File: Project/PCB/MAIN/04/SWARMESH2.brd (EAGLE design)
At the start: 75 x 75 mm, 47 parts, among them Q1 TIP122, U1 ESP32DEVKITC, U2 CD4051BEE4, U3 L293D, U4 L7805CV-DG, U5 TCRT5000L, U6 TCRT5000L

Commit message: update pcb 20:33
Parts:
- moved C5 16.9 mm to (21.9, 46.1)
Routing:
- net GND: track 481.8 -> 491.5 mm
- net ADCMX: track 49.3 -> 50.7 mm
- added copper zone on layer 16, net GND
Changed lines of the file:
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@@
 <attribute name="VALUE" x="53.972809375" y="12.749940625" size="2.08328125" layer="27" ratio="10" rot="SR0" display="off"/>
 </element>
-<element name="C5" library="adafruit" library_urn="urn:adsk.eagle:library:420" package="C025-030X050" package3d_urn="urn:adsk.eagle:package:6240322/1" value="" x="38.3667" y="42.4053" smashed="yes" rot="R90">
-<attribute name="NAME" x="36.4617" y="40.1193" size="1.27" layer="25" font="vector" ratio="15" rot="R90"/>
-<attribute name="VALUE" x="41.4147" y="40.1193" size="1.27" layer="27" ratio="10" rot="R90"/>
+<element name="C5" library="adafruit" library_urn="urn:adsk.eagle:library:420" package="C025-030X050" package3d_urn="urn:adsk.eagle:package:6240322/1" value="" x="21.9075" y="46.0629" smashed="yes" rot="R90">
+<attribute name="NAME" x="20.0025" y="43.7769" size="1.27" layer="25" font="vector" ratio="15" rot="R90"/>
+<attribute name="VALUE" x="24.9555" y="43.7769" size="1.27" layer="27" ratio="10" rot="R90"/>
 </element>
 <element name="C3" library="adafruit" library_urn="urn:adsk.eagle:library:420" package="C025-025X050" package3d_urn="urn:adsk.eagle:package:6240323/1" value="" x="58.42" y="70.8025" smashed="yes">
@@
 <wire x1="12.6746" y1="34.8742" x2="13.87145" y2="34.8742" width="0.635" layer="16"/>
 <wire x1="13.87145" y1="34.8742" x2="13.895325" y2="34.898075" width="0.635" layer="16"/>
-<wire x1="13.208" y1="41.4975" x2="21.415" y2="49.7045" width="0.635" layer="16"/>
-<wire x1="21.2725" y1="53.0225" x2="21.415" y2="52.88" width="0.635" layer="16"/>
-<wire x1="21.415" y1="52.88" x2="21.415" y2="49.7045" width="0.635" layer="16"/>
+<wire x1="13.208" y1="41.4975" x2="13.208" y2="45.1551" width="0.635" layer="16"/>
+<wire x1="21.2725" y1="53.0225" x2="21.0754" y2="53.0225" width="0.635" layer="16"/>
+<wire x1="21.0754" y1="53.0225" x2="13.208" y2="45.1551" width="0.635" layer="16"/>
 <wire x1="52.695" y1="33.9825" x2="52.705" y2="33.9725" width="0.635" layer="16"/>
 <wire x1="52.695" y1="33.9825" x2="51.235" y2="33.9825" width="0.635" layer="16"/>
@@
 <wire x1="58.7375" y1="44.1325" x2="59.055" y2="44.45" width="0.635" layer="16"/>
 <wire x1="59.055" y1="44.45" x2="62.23" y2="44.45" width="0.635" layer="16"/>
-<wire x1="38.3667" y1="43.6753" x2="44.4627" y2="43.6753" width="0.635" layer="16"/>
-<wire x1="50.0099" y1="49.2225" x2="44.4627" y2="43.6753" width="0.635" layer="16"/>
-<wire x1="50.0099" y1="49.2225" x2="51.235" y2="49.2225" width="0.635" layer="16"/>
+<wire x1="24.4067" y1="51.0513" x2="21.9075" y2="48.5521" width="0.635" layer="16"/>
+<wire x1="21.9075" y1="48.5521" x2="21.9075" y2="47.3329" width="0.635" layer="16"/>
+<wire x1="24.4067" y1="51.0513" x2="27.432" y2="51.0513" width="0.635" layer="16"/>
 <wire x1="41.1675" y1="36.83" x2="42.8625" y2="36.83" width="0.3048" layer="16"/>
 <wire x1="42.8625" y1="36.83" x2="43.5423" y2="36.1502" width="0.3048" layer="16"/>
@@
 <wire x1="41.1675" y1="8.255" x2="41.1675" y2="9.5551375" width="0.3048" layer="16"/>
 <wire x1="41.1675" y1="9.5551375" x2="39.4192375" y2="11.3034" width="0.3048" layer="16"/>
-<wire x1="21.2725" y1="53.0225" x2="23.0886" y2="51.2064" width="0.6096" layer="16"/>
-<wire x1="34.7091" y1="43.6753" x2="38.3667" y2="43.6753" width="0.6096" layer="16"/>
-<wire x1="34.7091" y1="43.6753" x2="27.178" y2="51.2064" width="0.6096" layer="16"/>
-<wire x1="23.0886" y1="51.2064" x2="27.178" y2="51.2064" width="0.6096" layer="16"/>
-<polygon width="0.3048" layer="1" spacing="0.0254" isolate="0.3048">
-<vertex x="55.4736" y="36.576"/>
-<vertex x="54.2544" y="35.3568"/>
-<vertex x="54.2544" y="15.8496"/>
-<vertex x="55.4736" y="14.6304"/>
-<vertex x="63.3984" y="14.6304"/>
-<vertex x="65.2272" y="16.4592"/>
-<vertex x="65.2272" y="35.3568"/>
-<vertex x="64.008" y="36.576"/>
-</polygon>
+<wire x1="21.2725" y1="53.0225" x2="21.9075" y2="52.3875" width="0.6096" layer="16"/>
+<wire x1="21.9075" y1="52.3875" x2="21.9075" y2="47.3329" width="0.6096" layer="16"/>
 <polygon width="0.3048" layer="1" spacing="0.0254" isolate="0.3048">
 <vertex x="49.3776" y="66.8528"/>
@@
 <vertex x="51.816" y="65.2272"/>
 </polygon>
+<polygon width="0.1524" layer="16" isolate="0.254">
+<vertex x="56.0832" y="35.9664"/>
+<vertex x="54.2544" y="34.1376"/>
+<vertex x="54.2544" y="15.8496"/>
+<vertex x="54.864" y="15.24"/>
+<vertex x="64.008" y="15.24"/>
+<vertex x="65.2272" y="16.4592"/>
+<vertex x="65.2272" y="35.3568"/>
+<vertex x="64.6176" y="35.9664"/>
+</polygon>
+<wire x1="27.432" y1="51.0513" x2="28.0416" y2="50.4417" width="0.6096" layer="16"/>
+<wire x1="28.0416" y1="50.4417" x2="28.0416" y2="48.768" width="0.6096" layer="16"/>
+<wire x1="28.0416" y1="48.768" x2="35.3568" y2="41.4528" width="0.6096" layer="16"/>
+<wire x1="35.3568" y1="41.4528" x2="40.8432" y2="41.4528" width="0.6096" layer="16"/>
+<wire x1="40.8432" y1="41.4528" x2="48.768" y2="49.3776" width="0.6096" layer="16"/>
+<wire x1="48.768" y1="49.3776" x2="51.0799" y2="49.3776" width="0.6096" layer="16"/>
+<wire x1="51.0799" y1="49.3776" x2="51.235" y2="49.2225" width="0.6096" layer="16"/>
 </signal>
 <signal name="VCC">
@@
 <wire x1="55.88" y1="29.5275" x2="52.695" y2="32.7125" width="0.3048" layer="16"/>
 <wire x1="49.75644375" y1="32.7125" x2="52.695" y2="32.7125" width="0.3048" layer="16"/>
-<wire x1="23.6828" y1="42.16864375" x2="23.6828" y2="46.75135625" width="0.3048" layer="16"/>
-<wire x1="23.6828" y1="46.75135625" x2="24.88394375" y2="47.9525" width="0.3048" layer="16"/>
 <wire x1="26.045" y1="39.0625" x2="26.045" y2="39.80644375" width="0.3048" layer="16"/>
 <wire x1="26.045" y1="39.80644375" x2="23.6828" y2="42.16864375" width="0.3048" layer="16"/>
-<wire x1="38.3667" y1="41.1353" x2="41.33364375" y2="41.1353" width="0.3048" layer="16"/>
-<wire x1="41.33364375" y1="41.1353" x2="49.75644375" y2="32.7125" width="0.3048" layer="16"/>
-<wire x1="34.0995" y1="41.1353" x2="38.3667" y2="41.1353" width="0.3048" layer="16"/>
-<wire x1="34.0995" y1="41.1353" x2="27.2823" y2="47.9525" width="0.3048" layer="16"/>
-<wire x1="24.88394375" y1="47.9525" x2="27.2823" y2="47.9525" width="0.3048" layer="16"/>
+<wire x1="41.94324375" y1="40.5257" x2="49.75644375" y2="32.7125" width="0.3048" layer="16"/>
+<wire x1="21.9075" y1="44.7929" x2="23.6828" y2="43.0176" width="0.3048" layer="16"/>
+<wire x1="23.6828" y1="43.0176" x2="23.6828" y2="42.16864375" width="0.3048" layer="16"/>
+<wire x1="25.51894375" y1="47.9525" x2="26.57105625" y2="47.9525" width="0.3048" layer="16"/>
+<wire x1="21.9075" y1="44.7929" x2="22.35934375" y2="44.7929" width="0.3048" layer="16"/>
+<wire x1="22.35934375" y1="44.7929" x2="25.51894375" y2="47.9525" width="0.3048" layer="16"/>
+<wire x1="26.57105625" y1="47.9525" x2="33.99785625" y2="40.5257" width="0.3048" layer="16"/>
+<wire x1="33.99785625" y1="40.5257" x2="41.94324375" y2="40.5257" width="0.3048" layer="16"/>
 </signal>
 <signal name="BATLVL">

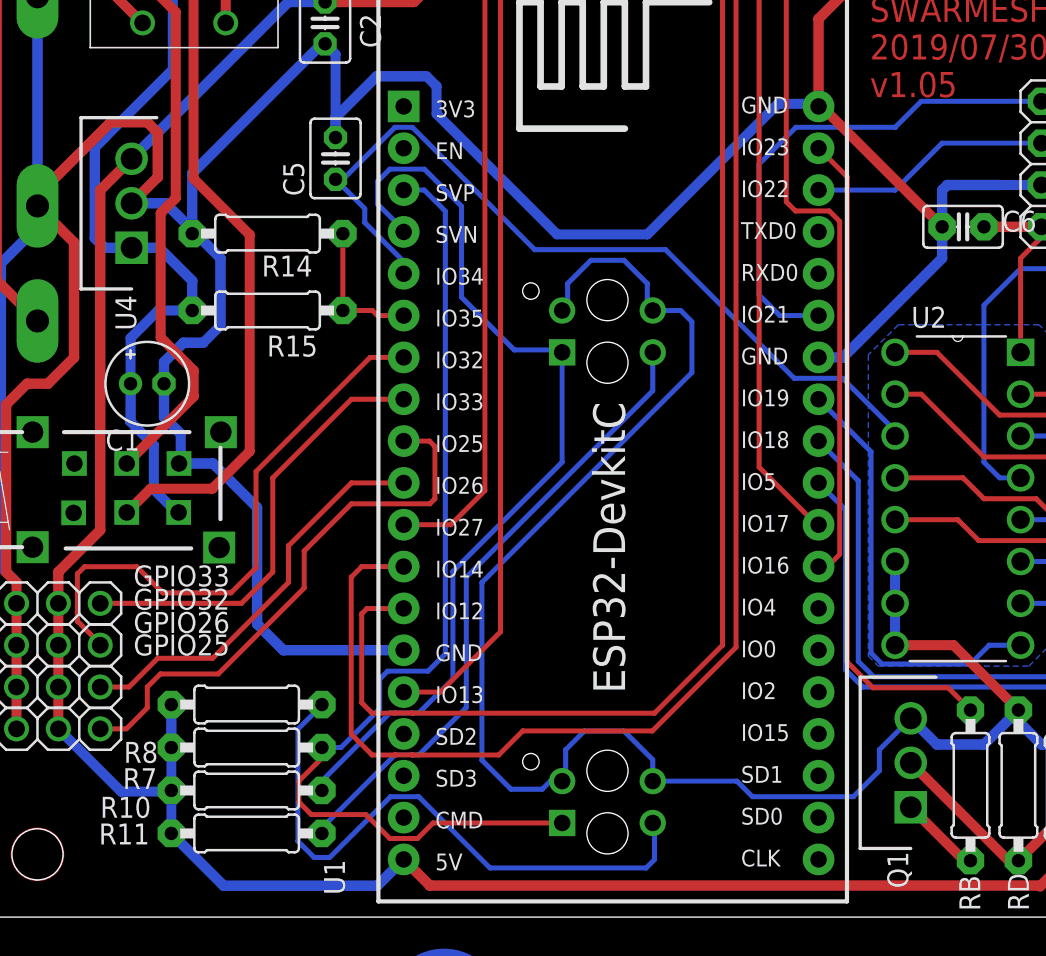
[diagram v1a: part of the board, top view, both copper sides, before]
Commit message: added 2nd version of IR pcb
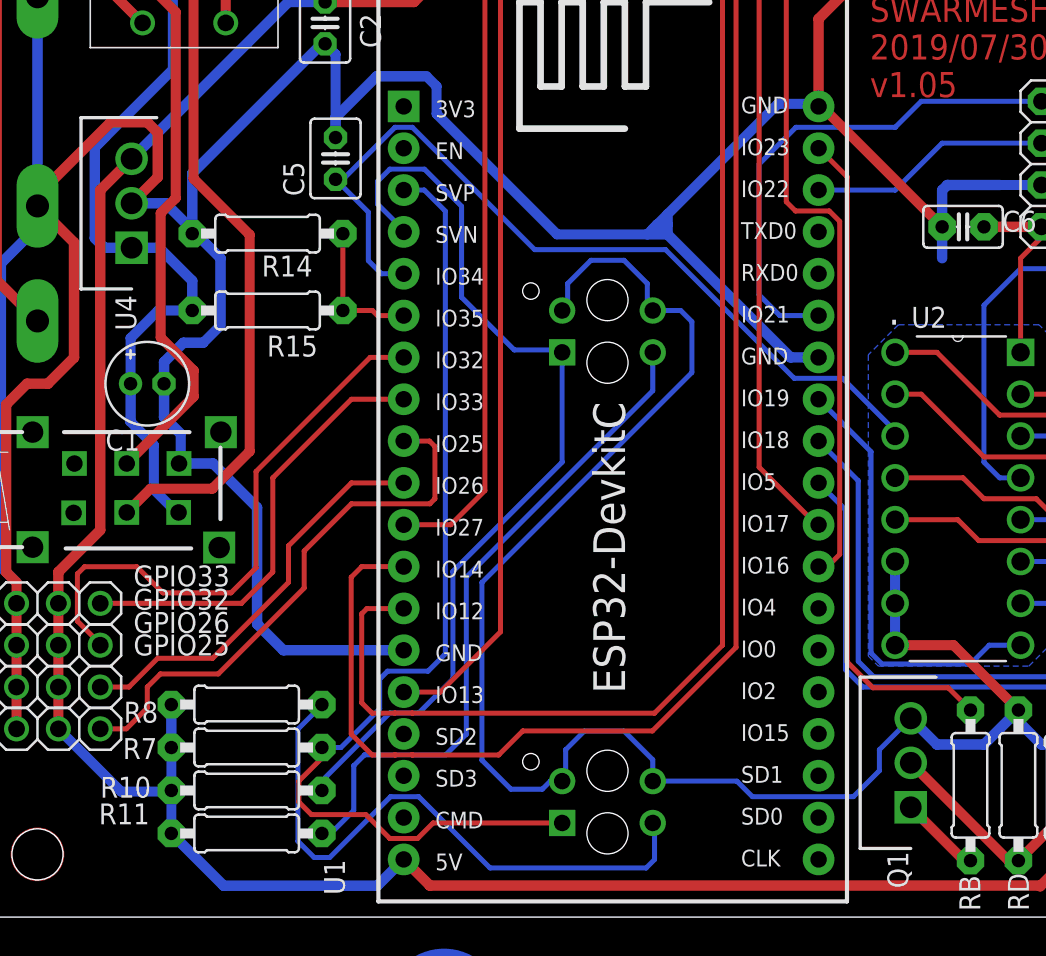
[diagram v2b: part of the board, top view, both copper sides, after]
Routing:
- net GND: track 491.5 -> 497.2 mm
- net N$9: track 38.4 -> 40.7 mm
- net ADCMX: track 50.7 -> 51.5 mm
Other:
- board text added: "."
